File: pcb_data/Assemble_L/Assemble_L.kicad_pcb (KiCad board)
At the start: 2 copper layers, 158.4 x 96.4 mm, 85 parts, among them J1 Conn_01x02, U1 XIAO-nRF52840

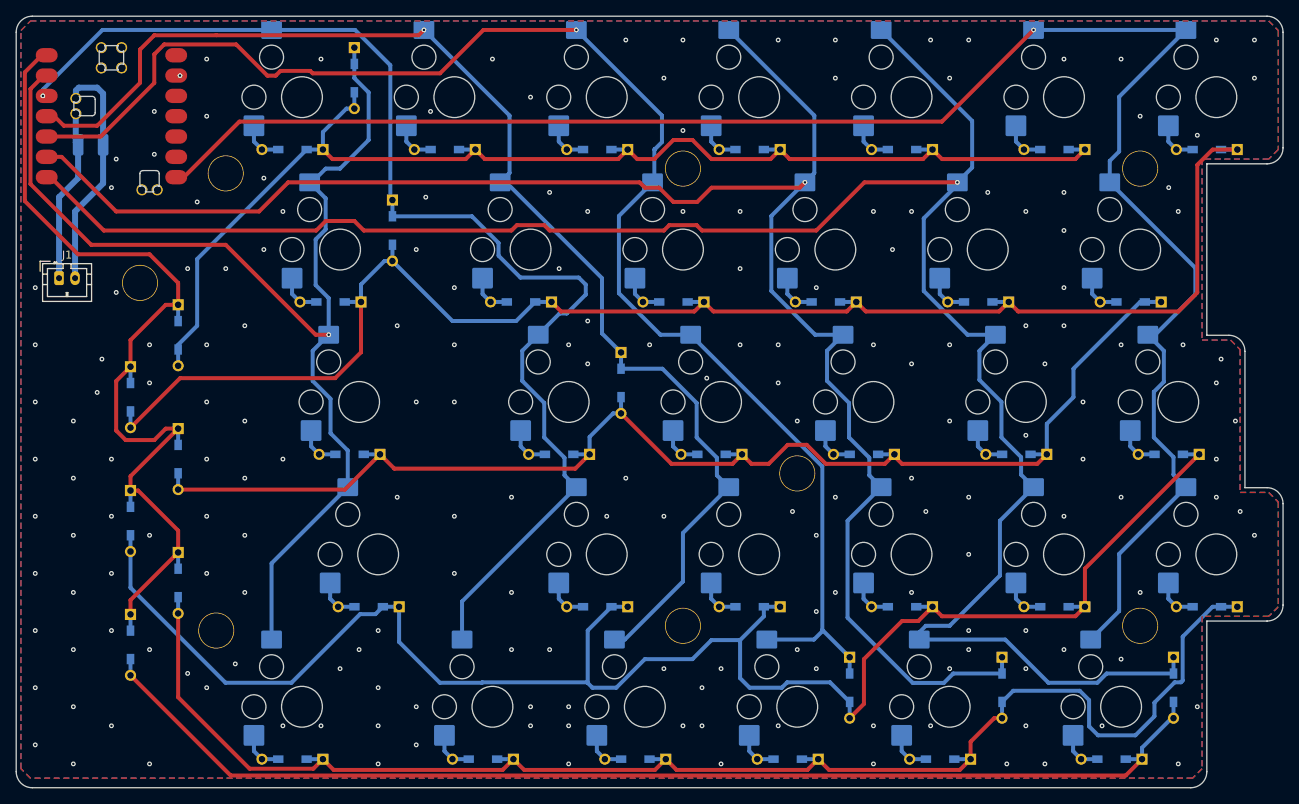
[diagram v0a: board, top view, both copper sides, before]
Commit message: Issue/15 top and bottom plate (#26)
* copy from Assemble

* remove file

* rename file

* remove file

* replace value

* fix position of mounting hole

* copy from Assemble_L

* remove segment and via

* remove zone

* remove diode

* replace switch footprint

* update line

* update footprint

* remove unnecessary footprint

* add step file

* change hole position

* step updated

* add bottom_l project file

* remove unnecessary footprint

* add step file

* copy from Assemble_R

* remove zone, segment and via

* remove diode

* replace switch footprint

* update line

* remove unnecessary footprint

* add step file

* add bottom_r project file

* remove unnecessary footprint

* add step file

* fix hole footprint and number (#25)

* fix line

* Issue/12 build guide (#28)

* add build guide

* update build guide

* Update docs/requirements/requirements_board.md

* Update docs/requirements/requirements_board.md

* Update docs/requirements/requirements_board.md

* Update docs/requirements/requirements_board.md

* Update docs/requirements/requirements_board.md

* Update docs/build_guide.md

* Update docs/build_guide.md

* Update README.md

* Update docs/build_guide.md

* Update docs/build_guide.md

* Update README.md

* Update docs/build_guide.md

* Update docs/build_guide.md

* Update docs/build_guide.md

* Update docs/build_guide.md

* Update docs/build_guide.md

* Update docs/build_guide.md

* Update docs/build_guide.md

* Update docs/build_guide.md

* Update docs/build_guide.md

* Update docs/build_guide.md

* Update docs/build_guide.md

* Update docs/build_guide.md

* Update docs/build_guide.md

* Update docs/build_guide.md

* Update docs/build_guide.md

* Update docs/build_guide.md

* Update docs/build_guide.md

* Update docs/build_guide.md

* Update docs/build_guide.md

* Update docs/build_guide.md

* Update docs/build_guide.md

* Update docs/build_guide.md

* Update docs/build_guide.md

* Update docs/build_guide.md

* Update docs/build_guide.md

* Update doc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
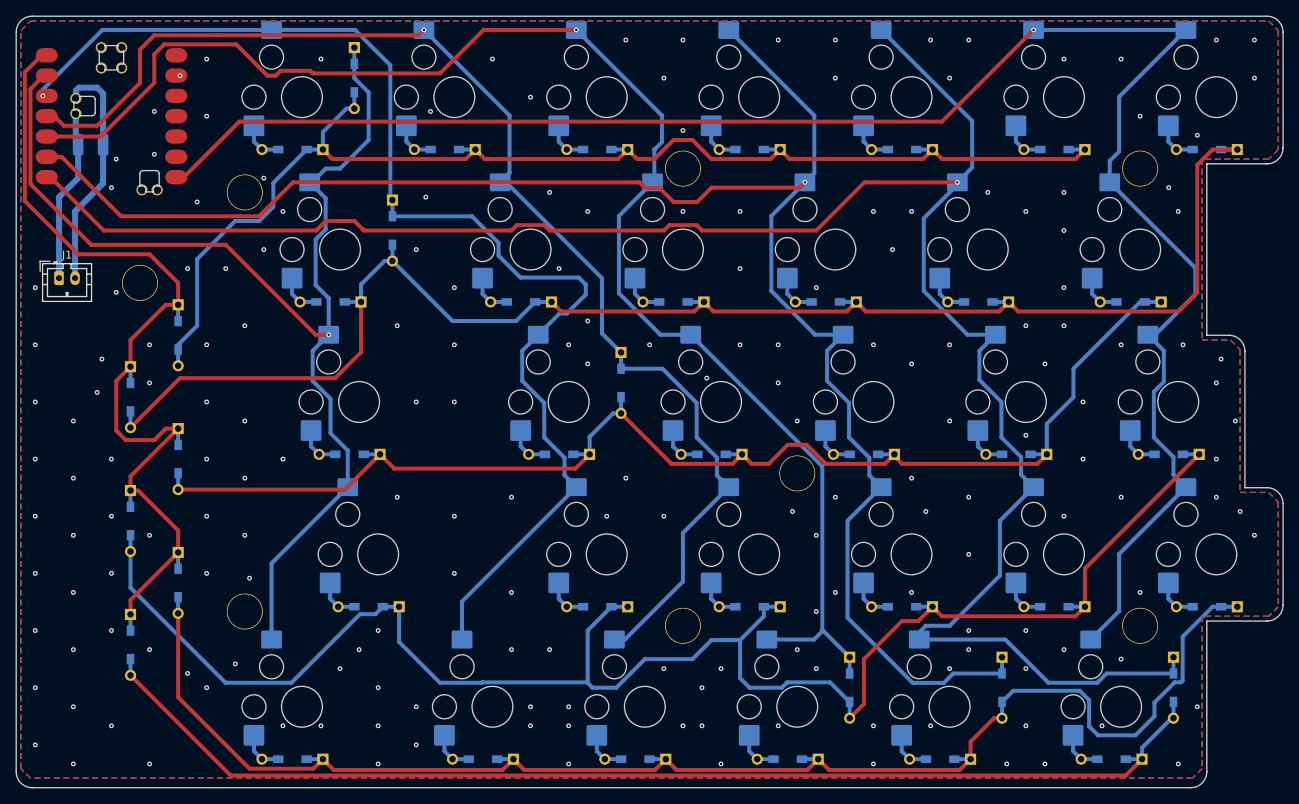
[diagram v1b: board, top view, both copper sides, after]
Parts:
- moved H4 4.29 mm to (73.8, 121.4)
- moved H1 3.37 mm to (73.8, 69.1)
- renumbered H8 to H7, H7 to H8
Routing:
- net Net-(D1-0-K): track 157.4 -> 159.2 mm
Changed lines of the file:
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@@
 		(descr "Mounting Hole 2.2mm, no annular, M2")
 		(tags "mounting hole 2.2mm no annular m2")
-		(property "Reference" "H7"
+		(property "Reference" "H8"
 			(at 0 -3.2 0)
 			(layer "F.Fab")
@@
 	(footprint "kbd_Hole:m2_Spacer_Hole"
 		(layer "F.Cu")
-		(at 71.43756 66.675056)
+		(at 73.818812 69.056308)
 		(descr "Mounting Hole 2.2mm, no annular, M2")
 		(tags "mounting hole 2.2mm no annular m2")
@@
 		(descr "Mounting Hole 2.2mm, no annular, M2")
 		(tags "mounting hole 2.2mm no annular m2")
-		(property "Reference" "H8"
+		(property "Reference" "H7"
 			(at 0 -3.2 0)
 			(layer "F.Fab")
@@
 	(footprint "kbd_Hole:m2_Spacer_Hole"
 		(layer "F.Cu")
-		(at 70.246934 123.825104)
+		(at 73.818812 121.443852)
 		(descr "Mounting Hole 2.2mm, no annular, M2")
 		(tags "mounting hole 2.2mm no annular m2")
@@
 	(gr_line
 		(start 201.597046 47.029727)
-		(end 47.24375 47.029727)
+		(end 47.243787 47.029727)
 		(stroke
 			(width 0.05)
@@
 	)
 	(gr_arc
-		(start 45.24375 49.029727)
-		(mid 45.82953 47.615514)
-		(end 47.24375 47.029727)
+		(start 45.243787 49.029727)
+		(mid 45.829573 47.615513)
+		(end 47.243787 47.029727)
 		(stroke
 			(width 0.05)
@@
 	)
 	(gr_line
-		(start 45.24375 49.029727)
+		(start 45.243787 49.029727)
 		(end 45.243787 141.470434)
 		(stroke
@@
 	)
 	(segment
-		(start 65.48443 88.106324)
-		(end 67.865682 85.725072)
+		(start 72.628186 72.628186)
+		(end 75.604751 72.628186)
 		(width 0.5)
 		(layer "B.Cu")
@@
 	)
 	(segment
-		(start 67.865682 77.379751)
-		(end 81.546942 63.698491)
+		(start 77.39069 67.865682)
+		(end 81.546942 63.70943)
 		(width 0.5)
 		(layer "B.Cu")
@@
 	)
 	(segment
+		(start 67.865682 77.379751)
+		(end 67.876621 77.379751)
+		(width 0.5)
+		(layer "B.Cu")
+		(net 10)
+	)
+	(segment
 		(start 87.511011 58.578796)
 		(end 87.511011 56.543796)
@@
 	)
 	(segment
+		(start 67.876621 77.379751)
+		(end 72.628186 72.628186)
+		(width 0.5)
+		(layer "B.Cu")
+		(net 10)
+	)
+	(segment
 		(start 81.546942 63.698491)
 		(end 83.581942 63.698491)
@@
 	)
 	(segment
+		(start 77.39069 70.842247)
+		(end 77.39069 67.865682)
+		(width 0.5)
+		(layer "B.Cu")
+		(net 10)
+	)
+	(segment
+		(start 75.604751 72.628186)
+		(end 77.39069 70.842247)
+		(width 0.5)
+		(layer "B.Cu")
+		(net 10)
+	)
+	(segment
+		(start 81.546942 63.70943)
+		(end 81.546942 63.698491)
+		(width 0.5)
+		(layer "B.Cu")
+		(net 10)
+	)
+	(segment
+		(start 65.48443 88.106324)
+		(end 67.865682 85.725072)
+		(width 0.5)
+		(layer "B.Cu")
+		(net 10)
+	)
+	(segment
 		(start 87.511011 58.578796)
 		(end 86.523183 58.578796)
@@
 	)
 	(segment
-		(start 143.176505 68.460995)
-		(end 143.8375 67.8)
+		(start 50.919051 64.61125)
+		(end 58.340674 72.032873)
 		(width 0.5)
 		(layer "F.Cu")
@@
 	)
 	(segment
-		(start 79.242311 67.8)
-		(end 123.164109 67.8)
+		(start 125.611043 68.460995)
+		(end 127.396982 70.246934)
 		(width 0.5)
 		(layer "F.Cu")
@@
 	)
 	(segment
-		(start 127.396982 70.246934)
-		(end 130.373547 70.246934)
+		(start 123.164109 67.8)
+		(end 123.825104 68.460995)
 		(width 0.5)
 		(layer "F.Cu")
@@
 	)
 	(segment
-		(start 125.611043 68.460995)
-		(end 127.396982 70.246934)
+		(start 143.176505 68.460995)
+		(end 143.8375 67.8)
 		(width 0.5)
 		(layer "F.Cu")
@@
 	)
 	(segment
-		(start 49.53 64.61125)
-		(end 50.919051 64.61125)
+		(start 58.340674 72.032873)
+		(end 75.604751 72.032873)
 		(width 0.5)
 		(layer "F.Cu")
@@
 	)
 	(segment
-		(start 132.159486 68.460995)
-		(end 143.176505 68.460995)
+		(start 123.825104 68.460995)
+		(end 125.611043 68.460995)
 		(width 0.5)
 		(layer "F.Cu")
@@
 	)
 	(segment
-		(start 123.164109 67.8)
-		(end 123.825104 68.460995)
+		(start 49.53 64.61125)
+		(end 50.919051 64.61125)
 		(width 0.5)
 		(layer "F.Cu")
@@
 	)
 	(segment
-		(start 123.825104 68.460995)
-		(end 125.611043 68.460995)
+		(start 127.396982 70.246934)
+		(end 130.373547 70.246934)
 		(width 0.5)
 		(layer "F.Cu")
@@
 	)
 	(segment
-		(start 75.604751 71.43756)
-		(end 79.242311 67.8)
+		(start 75.604751 72.032873)
+		(end 79.837624 67.8)
 		(width 0.5)
 		(layer "F.Cu")
@@
 	)
 	(segment
-		(start 57.745361 71.43756)
-		(end 75.604751 71.43756)
+		(start 132.159486 68.460995)
+		(end 143.176505 68.460995)
 		(width 0.5)
 		(layer "F.Cu")
@@
 	)
 	(segment
-		(start 50.919051 64.61125)
-		(end 57.745361 71.43756)
+		(start 79.837624 67.8)
+		(end 123.164109 67.8)
 		(width 0.5)
 		(layer "F.Cu")
@@
 	)
 	(via
-		(at 73.81875 119.0625)
+		(at 74.414125 117.276661)
 		(size 0.6)
 		(drill 0.3)
